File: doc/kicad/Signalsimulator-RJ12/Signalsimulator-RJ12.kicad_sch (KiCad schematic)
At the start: 15 parts, among them J1 Conn_02x03_Odd_Even, J2 RJ12, J3 RJ12

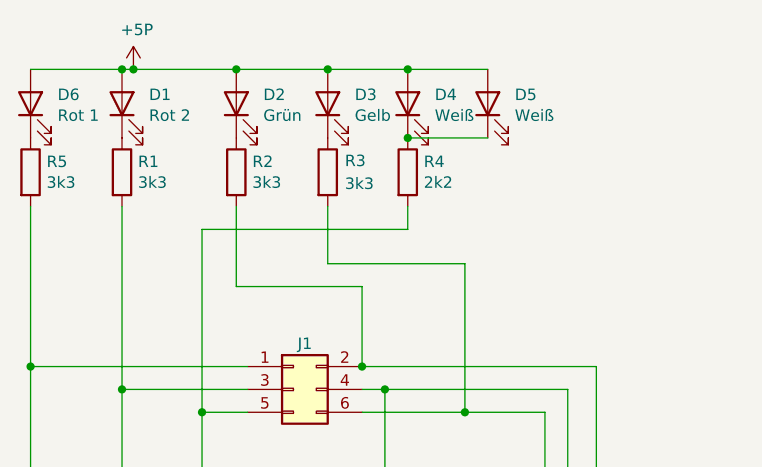
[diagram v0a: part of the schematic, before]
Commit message: Widerstandswerte angepasst
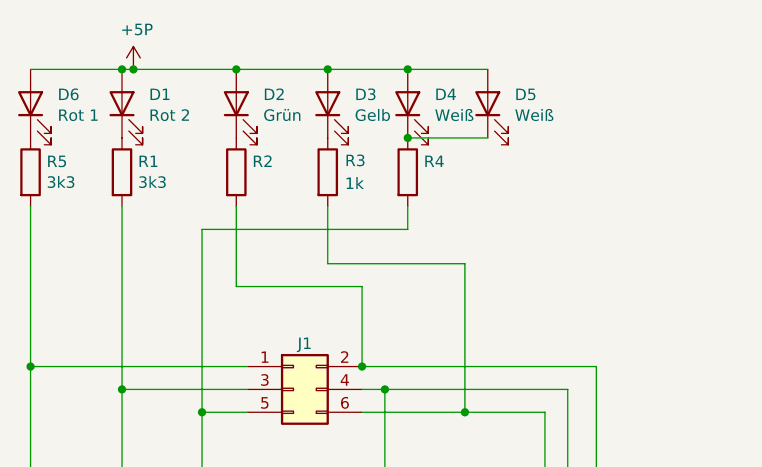
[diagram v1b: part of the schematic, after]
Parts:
- R2: value 3k3 -> (none)
- R4: value 2k2 -> (none)
- renumbered 3k3 to 1k
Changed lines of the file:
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@@
       (effects (font (size 1.27 1.27)) (justify left))
     )
-    (property "Value" "3k3" (id 1) (at 121.158 67.183 0)
+    (property "Value" "" (id 1) (at 121.158 67.183 0)
       (effects (font (size 1.27 1.27)) (justify left))
     )
@@
   (symbol (lib_id "Device:R") (at 129.54 66.04 0) (unit 1)
     (in_bom yes) (on_board yes)
-    (property "Reference" "3k3" (id 0) (at 131.445 67.31 0)
+    (property "Reference" "1k" (id 0) (at 131.445 67.31 0)
       (effects (font (size 1.27 1.27)) (justify left))
     )
@@
       (effects (font (size 1.27 1.27)) (justify left))
     )
-    (property "Value" "2k2" (id 1) (at 140.208 67.183 0)
+    (property "Value" "" (id 1) (at 140.208 67.183 0)
       (effects (font (size 1.27 1.27)) (justify left))
     )
@@
     )
     (path "/00000000-0000-0000-0000-0000607a4631"
-      (reference "3k3") (unit 1) (value "R3") (footprint "Resistors_THT:R_Axial_DIN0204_L3.6mm_D1.6mm_P7.62mm_Horizontal")
+      (reference "1k") (unit 1) (value "R3") (footprint "Resistors_THT:R_Axial_DIN0204_L3.6mm_D1.6mm_P7.62mm_Horizontal")
     )
     (path "/00000000-0000-0000-0000-0000607a062e"
@@
     )
     (path "/00000000-0000-0000-0000-0000607a3a5b"
-      (reference "R2") (unit 1) (value "3k3") (footprint "Resistors_THT:R_Axial_DIN0204_L3.6mm_D1.6mm_P7.62mm_Horizontal")
+      (reference "R2") (unit 1) (value "1k") (footprint "Resistors_THT:R_Axial_DIN0204_L3.6mm_D1.6mm_P7.62mm_Horizontal")
     )
     (path "/00000000-0000-0000-0000-0000607a4eab"
-      (reference "R4") (unit 1) (value "2k2") (footprint "Resistors_THT:R_Axial_DIN0204_L3.6mm_D1.6mm_P7.62mm_Horizontal")
+      (reference "R4") (unit 1) (value "10k") (footprint "Resistors_THT:R_Axial_DIN0204_L3.6mm_D1.6mm_P7.62mm_Horizontal")
     )
     (path "/00000000-0000-0000-0000-0000607b3367"
